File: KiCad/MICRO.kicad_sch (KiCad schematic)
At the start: 15 parts, among them J2 DE9_Pins, J4 DE9_Pins, J8 Conn_PIC_ICSP_ICD, U2 SN65HVD232, U7 PIC32MX250F128D-IPT, Y1 Crystal

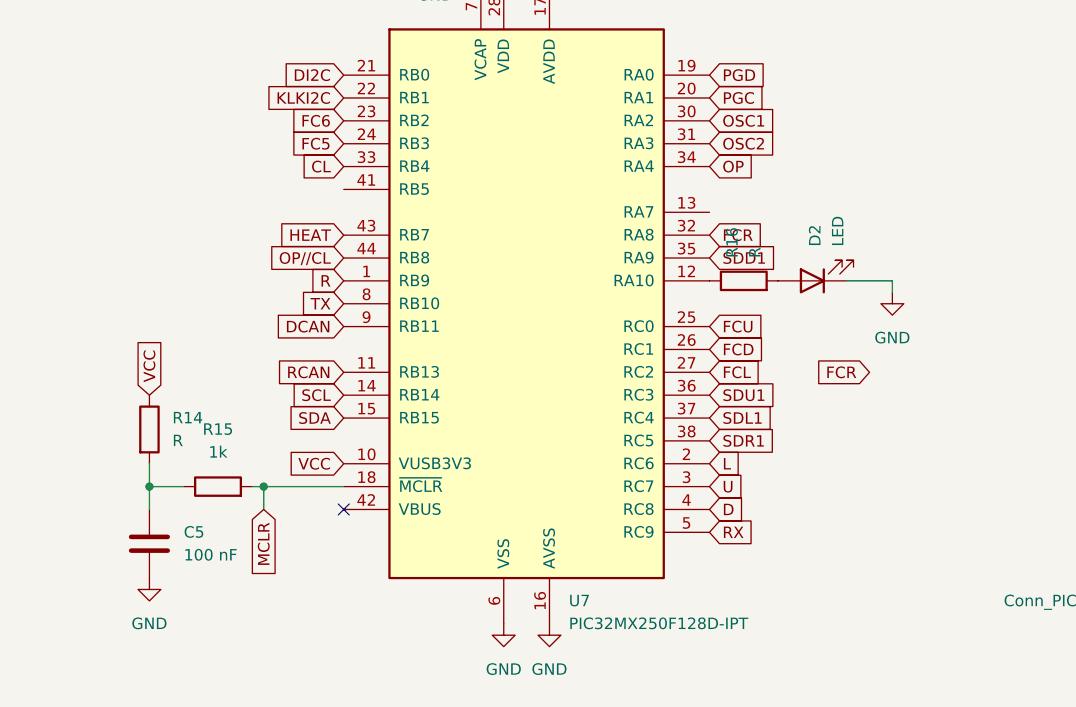
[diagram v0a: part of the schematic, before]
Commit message: routing V1.0 y recolocado algunos pines del Micro para eliminar islas//malas conexiones que no habia previsto
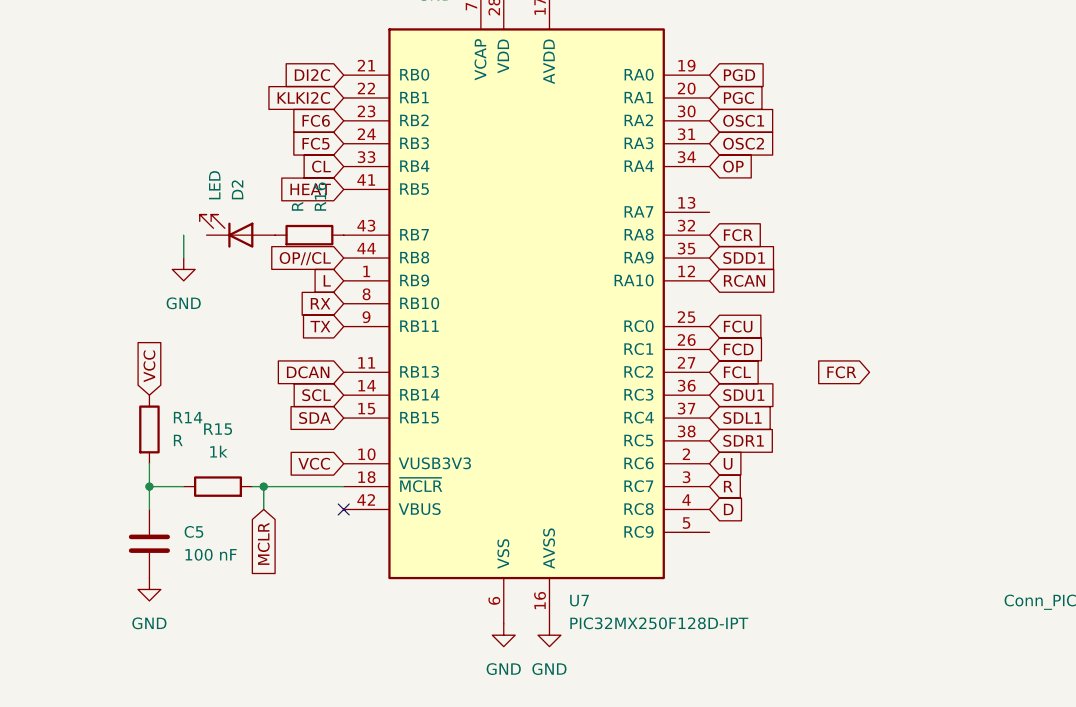
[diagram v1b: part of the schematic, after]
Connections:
- net DCAN: now also U7.11 (RB13); no longer U7.9 (RB11)
- net GND: no longer D2.1 (K)
- net HEAT: now also U7.41 (RB5); no longer U7.43 (RB7)
- net L: now also U7.1 (RB9); no longer U7.2 (RC6)
- net R: now also U7.3 (RC7); no longer U7.1 (RB9)
- net RCAN: now also U7.12 (RA10); no longer U7.11 (RB13)
- net RX: now also U7.8 (RB10); no longer U7.5 (RC9)
- net TX: now also U7.9 (RB11); no longer U7.8 (RB10)
- net U: now also U7.2 (RC6); no longer U7.3 (RC7)
- net at R16.1: now also U7.43 (RB7); no longer U7.12 (RA10)
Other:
- moved on the sheet: D2, R16

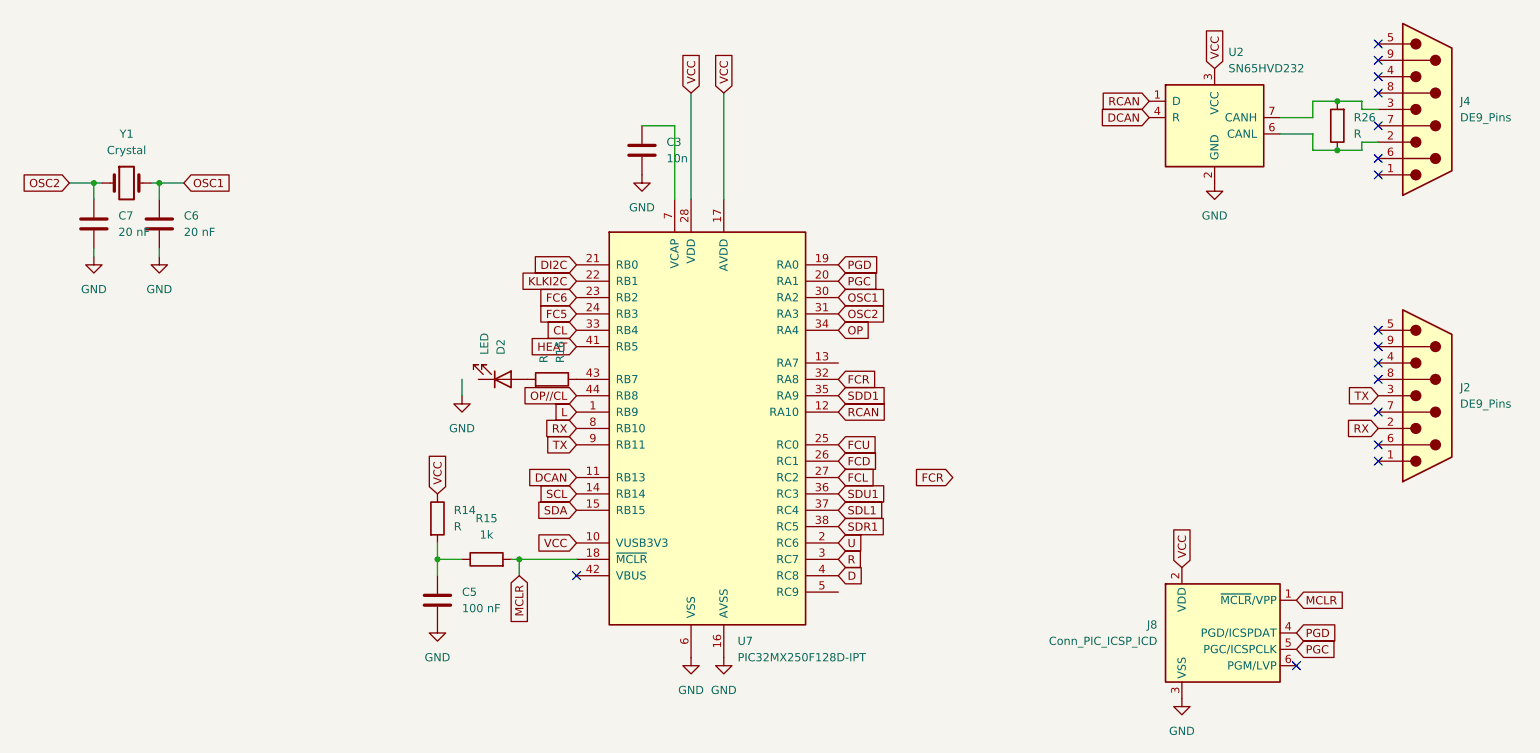
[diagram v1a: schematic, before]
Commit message: he corretgit un error en l'asignasio de pins del micro el qu eha fet que el routing y el placement canviin una mica
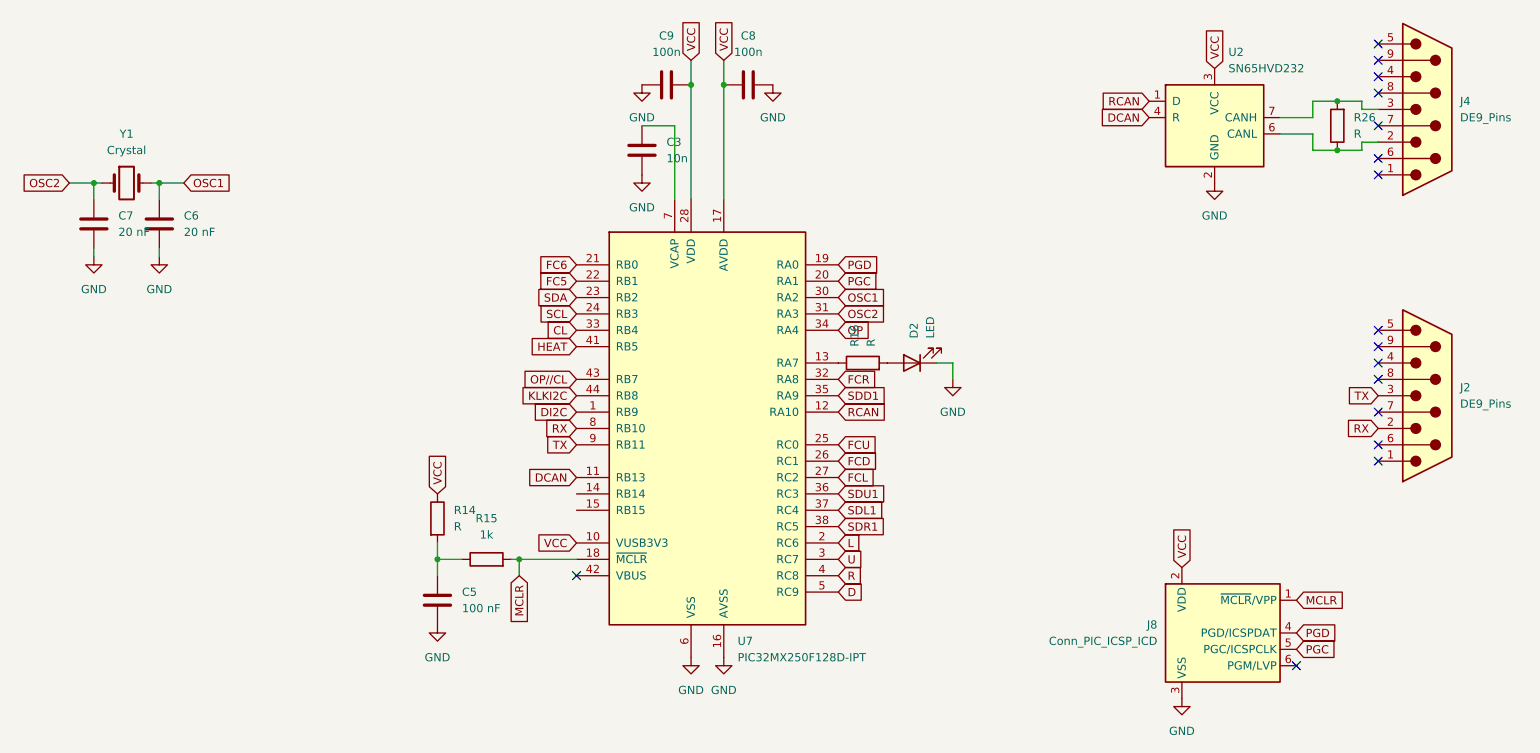
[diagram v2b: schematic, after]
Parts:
- added C8, C9: 100n, Capacitor_SMD:C_0402_1005Metric, symbol Device:C
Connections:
- net D: now also U7.5 (RC9); no longer U7.4 (RC8)
- net DI2C: now also U7.1 (RB9); no longer U7.21 (RB0)
- net FC5: now also U7.22 (RB1); no longer U7.24 (RB3)
- net FC6: now also U7.21 (RB0); no longer U7.23 (RB2)
- net GND: now also D2.1 (K), C8.1, C9.2
- net KLKI2C: now also U7.44 (RB8); no longer U7.22 (RB1)
- net L: now also U7.2 (RC6); no longer U7.1 (RB9)
- net OP//CL: now also U7.43 (RB7); no longer U7.44 (RB8)
- net R: now also U7.4 (RC8); no longer U7.3 (RC7)
- net SCL: now also U7.24 (RB3); no longer U7.14 (RB14)
- net SDA: now also U7.23 (RB2); no longer U7.15 (RB15)
- net U: now also U7.3 (RC7); no longer U7.2 (RC6)
- net VCC: now also C8.2, C9.1
- net at U7.13 (RA7): now also R16.1
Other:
- moved on the sheet: D2, R16

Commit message: versión casi final del enrutado
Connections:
- net CAN_-: now reaches J4.2, R26.1, U2.6 (CANL)
- net CAN_+: now reaches J4.3, R26.2, U2.7 (CANH)
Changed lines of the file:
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@@
+		)
+	)
+	(global_label "CAN_-"
+		(shape input)
+		(at 238.76 46.99 270)
+		(fields_autoplaced yes)
+		(effects
+			(font
+				(size 1.27 1.27)
+			)
+			(justify right)
+		)
+		(property "Intersheetrefs" "${INTERSHEET_REFS}"
+			(at 238.76 56.2043 90)
+			(effects
+				(font
+					(size 1.27 1.27)
+				)
+				(justify right)
+				(hide yes)
+			)
 		)
 	)
@@
 			(effects
 				(font
+					(size 1.27 1.27)
+				)
+				(justify left)
+				(hide yes)
+			)
+		)
+	)
+	(global_label "CAN_+"
+		(shape input)
+		(at 238.76 39.37 90)
+		(fields_autoplaced yes)
+		(effects
+			(font
+				(size 1.27 1.27)
+			)
+			(justify left)
+		)
+		(property "Intersheetrefs" "${INTERSHEET_REFS}"
+			(at 238.76 30.1557 90)
+			(effects
+				(font

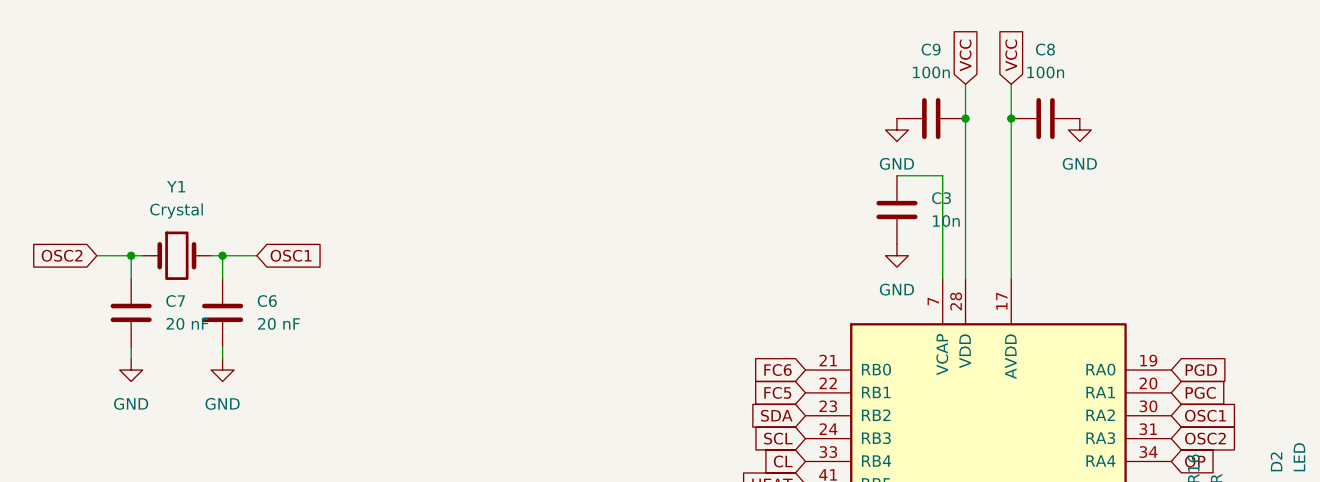
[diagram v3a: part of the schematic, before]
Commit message: añadido test points y solucionado un error con gnd en alimentación
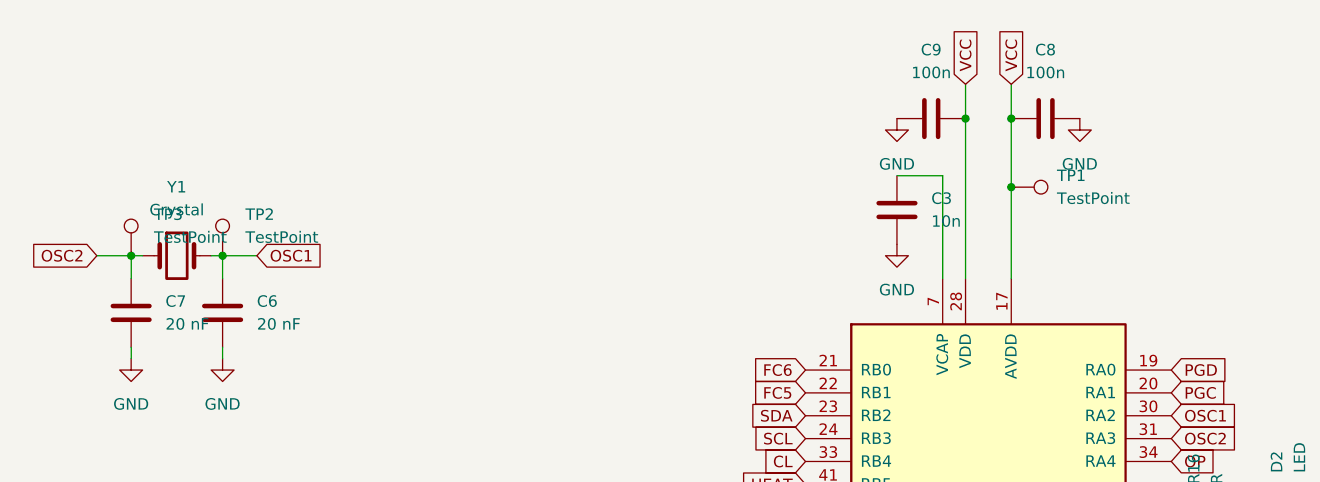
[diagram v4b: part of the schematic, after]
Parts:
- added TP1, TP2, TP3: TestPoint, TestPoint:TestPoint_Bridge_Pitch2.0mm_Drill0.7mm, symbol Connector:TestPoint
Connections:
- net OSC1: now also TP2.1
- net OSC2: now also TP3.1
- net VCC: now also TP1.1
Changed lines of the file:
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@@
+	)
+	(junction
+		(at 146.05 44.45)
+		(diameter 0)
+		(color 0 0 0 0)
 	)
 	(junction
@@
 	(wire
 		(pts
-			(xy 146.05 36.83) (xy 146.05 54.61)
+			(xy 146.05 36.83) (xy 146.05 44.45)
 		)
 		(stroke
@@
 		(pts
 			(xy 48.26 52.07) (xy 48.26 54.61)
+		)
+		(stroke
+			(width 0)
+			(type default)
+		)
+	)
+	(wire
+		(pts
+			(xy 146.05 44.45) (xy 146.05 54.61)
 		)
 		(stroke
@@
 	)
 	(symbol
+		(lib_id "Connector:TestPoint")
+		(at 146.05 44.45 270)
+		(unit 1)
+		(exclude_from_sim no)
+		(in_bom yes)
+		(on_board yes)
+		(dnp no)
+		(fields_autoplaced yes)
+		(property "Reference" "TP1"
+			(at 151.13 43.1799 90)
+			(effects
+				(font
+					(size 1.27 1.27)
+				)
+				(justify left)
+			)
+		)
+		(property "Value" "TestPoint"
+			(at 151.13 45.7199 90)
+			(effects
+				(font
+					(size 1.27 1.27)
+				)
+				(justify left)
+			)
+		)
+		(property "Footprint" "TestPoint:TestPoint_Bridge_Pitch2.0mm_Drill0.7mm"
+			(at 146.05 49.53 0)
+			(effects
+				(font
+					(size 1.27 1.27)
+				)
+				(hide yes)
+			)
+		)
+		(property "Datasheet" "~"
+			(at 146.05 49.53 0)
+			(effects
+				(font
+					(size 1.27 1.27)
+				)
+				(hide yes)
+			)
+		)
+		(property "Description" "test point"
+			(at 146.05 44.45 0)
+			(effects
+				(font
+					(size 1.27 1.27)
+				)
+				(hide yes)
+			)
+		)
+		(pin "1"
+		)
+		(instances
+			(project ""
+				(path "/9b9f005f-0621-4675-bd4e-683e7082b120/2f39354d-8df5-4269-96cb-5875be0a8958"
+					(reference "TP1")
+					(unit 1)
+				)
+			)
+		)
+	)
+	(symbol
 		(lib_id "Device:R")
 		(at 241.3 43.18 180)
@@
 	)
 	(symbol
+		(lib_id "Connector:TestPoint")
+		(at 58.42 52.07 0)
+		(unit 1)
+		(exclude_from_sim no)
+		(in_bom yes)
+		(on_board yes)
+		(dnp no)
+		(fields_autoplaced yes)
+		(property "Reference" "TP2"
+			(at 60.96 47.4979 0)
+			(effects
+				(font
+					(size 1.27 1.27)
+				)
+				(justify left)
+			)
+		)
+		(property "Value" "TestPoint"
+			(at 60.96 50.0379 0)
+			(effects
+				(font
+					(size 1.27 1.27)
+				)
+				(justify left)
+			)
+		)
+		(property "Footprint" "TestPoint:TestPoint_Bridge_Pitch2.0mm_Drill0.7mm"
+			(at 63.5 52.07 0)
+			(effects
+				(font
+					(size 1.27 1.27)
+				)
+				(hide yes)
+			)
+		)
+		(property "Datasheet" "~"
+			(at 63.5 52.07 0)
+			(effects
+				(font
+					(size 1.27 1.27)
+				)
+				(hide yes)
+			)
+		)
+		(property "Description" "test point"
+			(at 58.42 52.07 0)
+			(effects
+				(font
+					(size 1.27 1.27)
+				)
+				(hide yes)
+			)
+		)
+		(pin "1"
+		)
+		(instances
+			(project "Retrovisores"
+				(path "/9b9f005f-0621-4675-bd4e-683e7082b120/2f39354d-8df5-4269-96cb-5875be0a8958"
+					(reference "TP2")
+					(unit 1)
+				)
+			)
+		)
+	)
+	(symbol
 		(lib_id "power:GND")
 		(at 48.26 63.5 0)
@@
 					(unit 1)
 				)
+			)
+		)
+	)
+	(symbol
+		(lib_id "Connector:TestPoint")
+		(at 48.26 52.07 0)
+		(unit 1)
+		(exclude_from_sim no)
+		(in_bom yes)
+		(on_board yes)
+		(dnp no)
+		(fields_autoplaced yes)
+		(property "Reference" "TP3"
+			(at 50.8 47.4979 0)
+			(effects
+				(font
+					(size 1.27 1.27)
+				)
+				(justify left)
+			)
+		)
+		(property "Value" "TestPoint"
+			(at 50.8 50.0379 0)
+			(effects
+				(font
+					(size 1.27 1.27)
+				)
+				(justify left)
+			)
+		)
+		(property "Footprint" "TestPoint:TestPoint_Bridge_Pitch2.0mm_Drill0.7mm"
+			(at 53.34 52.07 0)
+			(effects
+				(font
+					(size 1.27 1.27)
+				)
+				(hide yes)
+			)
+		)
+		(property "Datasheet" "~"
+			(at 53.34 52.07 0)
+			(effects
+				(font
+					(size 1.27 1.27)
+				)
+				(hide yes)
+			)
+		)
+		(property "Description" "test point"
+			(at 48.26 52.07 0)
+			(effects
+				(font
+					(size 1.27 1.27)
+				)
+				(hide yes)
+			)
+		)
+		(pin "1"
+		)
+		(instances
+			(project "Retrovisores"
+				(path "/9b9f005f-0621-4675-bd4e-683e7082b120/2f39354d-8df5-4269-96cb-5875be0a8958"
+					(reference "TP3")
+					(unit 1)
+				)

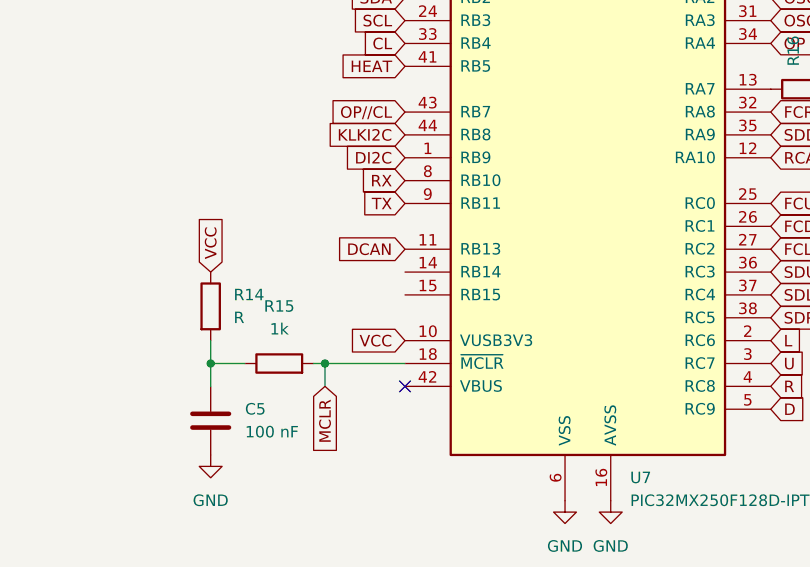
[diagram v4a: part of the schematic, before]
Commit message: mosfet bien colocados
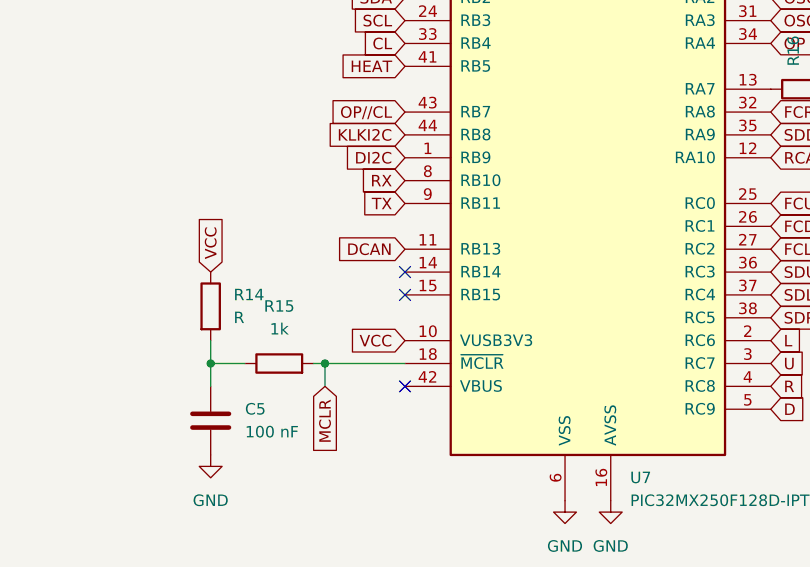
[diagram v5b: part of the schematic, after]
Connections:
- no-connect marks 16 -> 18
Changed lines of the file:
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@@
+	)
+	(no_connect
+		(at 123.19 100.33)
 	)
 	(no_connect
@@
 	)
 	(no_connect
+		(at 123.19 102.87)
+	)
+	(no_connect
